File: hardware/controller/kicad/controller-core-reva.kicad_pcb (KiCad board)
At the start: 2 copper layers, 141.6 x 135.2 mm, 159 parts, among them J101 12V_ISOLATED_INPUT / JST XH, J102 STM_SWD / 1x6 2.54mm, J103 ESP_UART / 1x6 2.54mm, J104 UI_LINK / IDC 2x8 2.54mm, J105 JP13 NTC / 2 vías, J106 JP5 FLOW ADAPTER / VCC-GND-OC, J107 JP14 DOOR / contacto seco, J108 JP16 VISUAL V1..V8 / XH-8, J109 JP22 WATER / RED-WHITE-BLACK, J110 USB-C SERVICE / USB 2.0, J111 USB BENCH POWER / OPEN, J112 24V_ACTUATOR_INPUT / JST XH, J113 JP3 VALVE / JST XH, J114 POWER MONITOR / MEASURE ONLY, J115 JP8 GRINDER / 320VDC, J117 JP24 PUMP / 230VAC, J118 JP17 MAINS / L-N, J121 24V INTERNAL SELECT / OPEN FO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, K701 G5RL-1A-E-TV8 DC24, Q501 SI2308A, Q701 SI2308A / relay coil, U101 STM32G431RBT6, U201 ESP32-S3-WROOM-1U-N8R8, U203 USBLC6-2SC6, U301 AP63203WU-7, U302 TPS22918DBVR, U303 AP63200WU-7 / 24V to 12V, U501 DRV8876PWPR, U502 UCC27517DBVR, U601 TPS3828-33DBVR, U602 SN74LVC2G08DCTR, U603 SN74LVC2G08DCTR

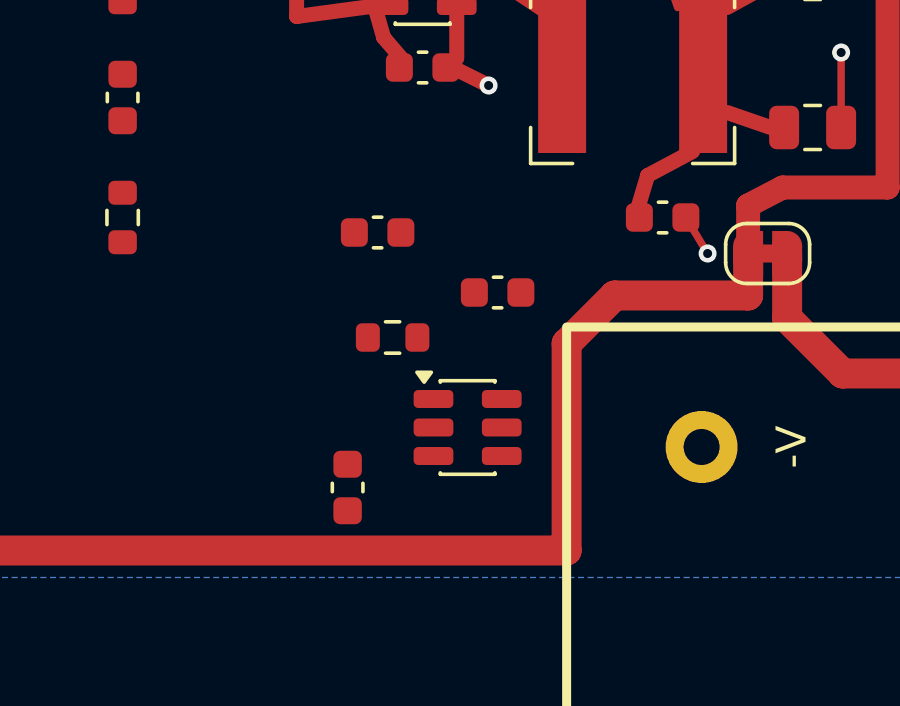
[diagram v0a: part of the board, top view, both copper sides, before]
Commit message: Route the front-panel load switch
PS701's footprint closes the pocket around U302 at x = 101.25 mm, so C307, C308
and C309 move west and north of the switch. C307 sets the rise time and sat
8 mm from pin 4; it is now beside it. The 3.3 V rail reaches the pocket along
y = 43 mm and down the free column at x = 91.6 mm.

DRC clean; 117 connections remain, down from 128.

Co-Authored-By: Claude Opus 5 <noreply@anthropic.com>
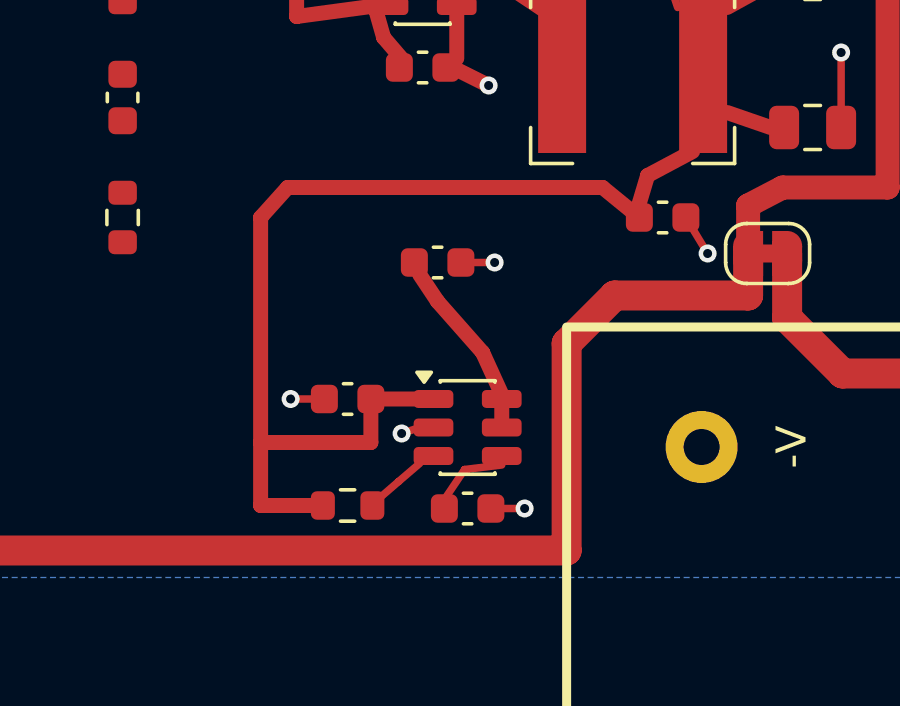
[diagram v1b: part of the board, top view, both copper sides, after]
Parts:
- moved C307 9.68 mm to (98.5, 53.7)
- moved R301 5.80 mm to (94.5, 53.6)
- moved C308 2.95 mm to (94.5, 50.0), turned to 180 degrees
- moved C309 2.24 mm to (97.5, 45.5)
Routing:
- net /3V3_CORE: track 112.4 -> 143.0 mm
- net /3V3_UI: track 0.00 -> 5.84 mm
- net /GND_UI: track 119.2 -> 123.2 mm, vias 70 -> 74
- net /UI_RISE: track 0.00 -> 2.45 mm
- net /UI_PWR_EN: track 0.00 -> 2.14 mm

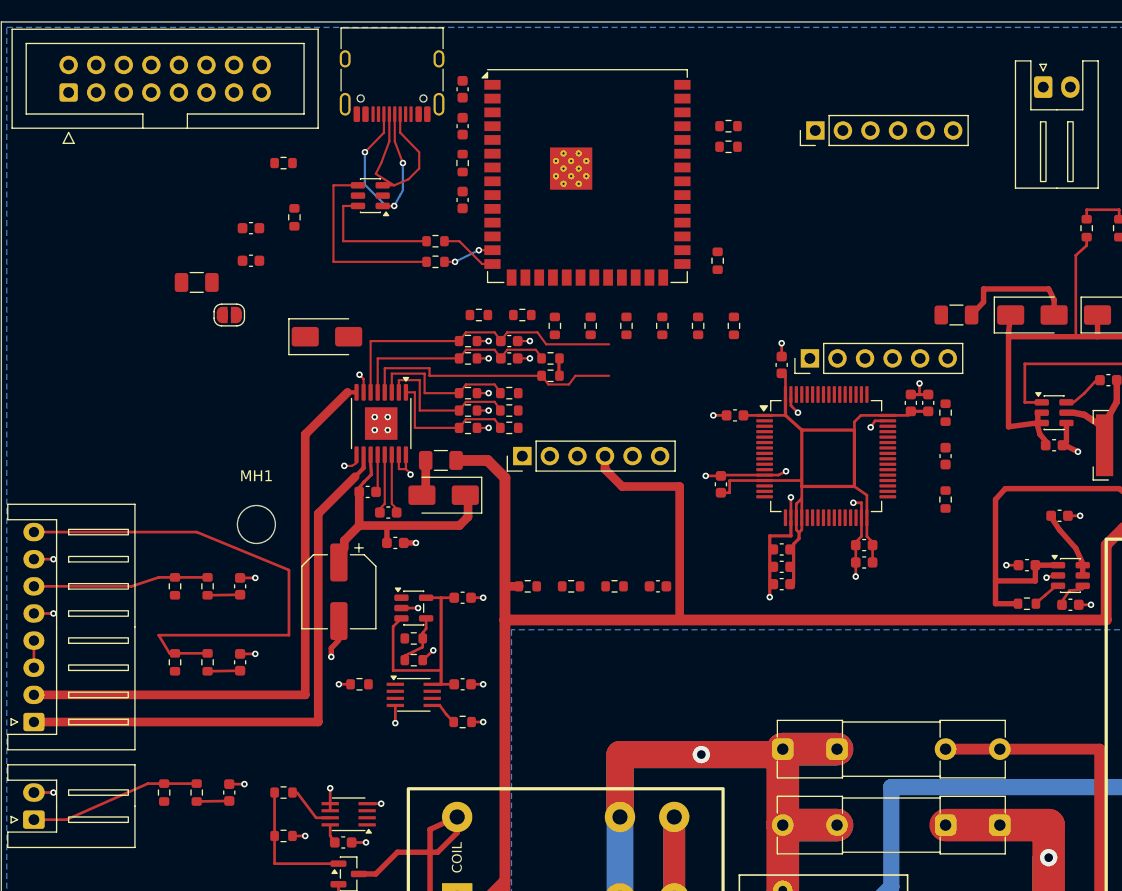
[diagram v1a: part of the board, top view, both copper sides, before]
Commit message: Distribute 3.3 V and ground the logic pins
One line leaves the buck along y = 43 mm and splits. The northern branch climbs
the gap between F301 and D301, runs over the ESP32 at y = 2.5 mm and feeds its
supply pins, its strap resistors and the UART header, plus the STM32 reset
pull-up and the SWD header. To free that gap, F301 moves 3 mm west and the
fused 12 V link passes under D301's body on B.Cu instead of round it.

The western branch runs in the 1.1 mm gap between the supervisor capacitors and
the 24 V trunk, passing under two 24 V branches on B.Cu, and reaches the
measurement header, the supervisor block, the arm gate and the contact and door
pull-ups. R405 turns 270 degrees so its supply pad faces north, clear of the
door harness lane.

Also drop the USB and ESP32 ground pins into the plane.

DRC clean; 90 connections remain, down from 117.

Co-Authored-By: Claude Opus 5 <noreply@anthropic.com>
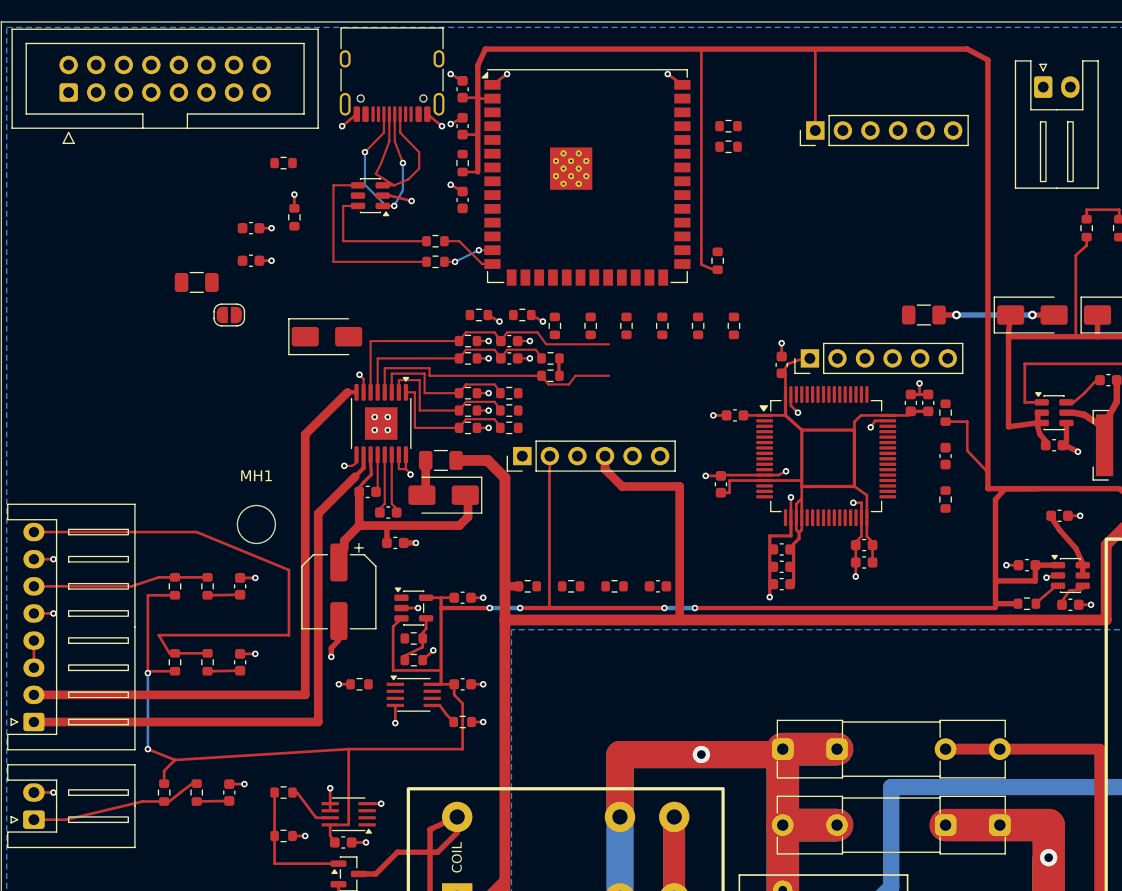
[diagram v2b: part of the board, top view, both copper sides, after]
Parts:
- moved F301 3.00 mm to (85.0, 27.0)
- turned R405 to -90 degrees
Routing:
- net /3V3_CORE: track 143.0 -> 414.9 mm, vias 0 -> 6
- net /GND_UI: track 123.2 -> 141.9 mm, vias 74 -> 87
- net /DOOR_RAW: track 15.7 -> 14.9 mm
- net /12V_FUSED: track 11.3 -> 10.6 mm, vias 0 -> 2

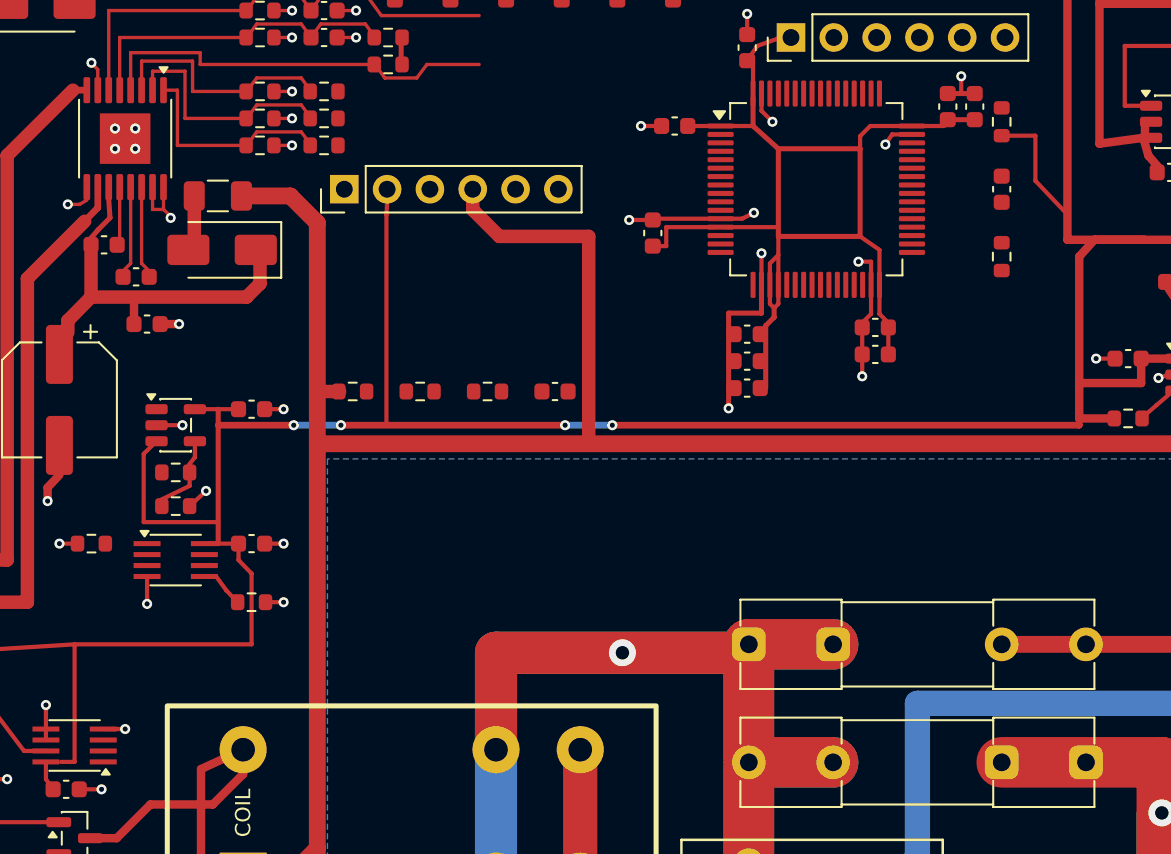
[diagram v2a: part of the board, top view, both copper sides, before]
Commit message: Route the reset tree
R101 and C101 sat east of the STM32, but its reset is pin 7 on the west side,
so the pair moves into the reset net's own corridor beside the supervisor that
drives it. The pin leaves flat, because the west pads are on a 0.5 mm pitch and
any diagonal touches its neighbour, drops to y = 50.5 mm and crosses west under
both 24 V branches into the 1.35 mm channel that was left empty for it.

Two reset points stay open and are documented: U602 pin 6, whose only approach
is the 0.87 mm gap east of the package that the valve arm net already uses, and
the SWD header's reset pin, which would have to cross the decoupling link north
of the MCU. Neither blocks debugging or start-up.

DRC clean; 85 connections remain.

Co-Authored-By: Claude Opus 5 <noreply@anthropic.com>
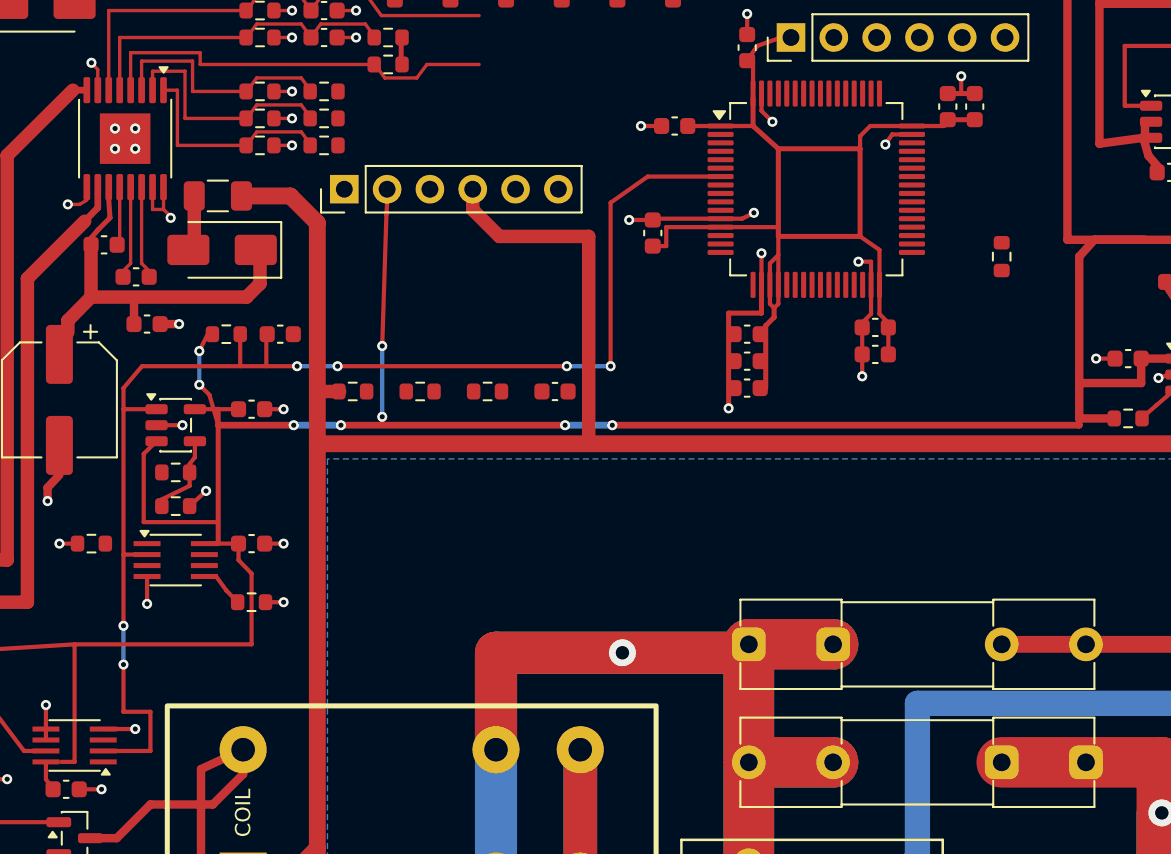
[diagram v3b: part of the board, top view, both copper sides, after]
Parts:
- moved R101 47.7 mm to (41.0, 48.6), turned to 0 degrees
- moved C101 43.7 mm to (44.2, 48.6), turned to 0 degrees
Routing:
- net /STM_NRST: track 0.00 -> 76.4 mm, vias 0 -> 6
- net /3V3_CORE: track 414.9 -> 413.7 mm, vias 6 -> 10
- net /GND_UI: track 141.9 -> 142.5 mm

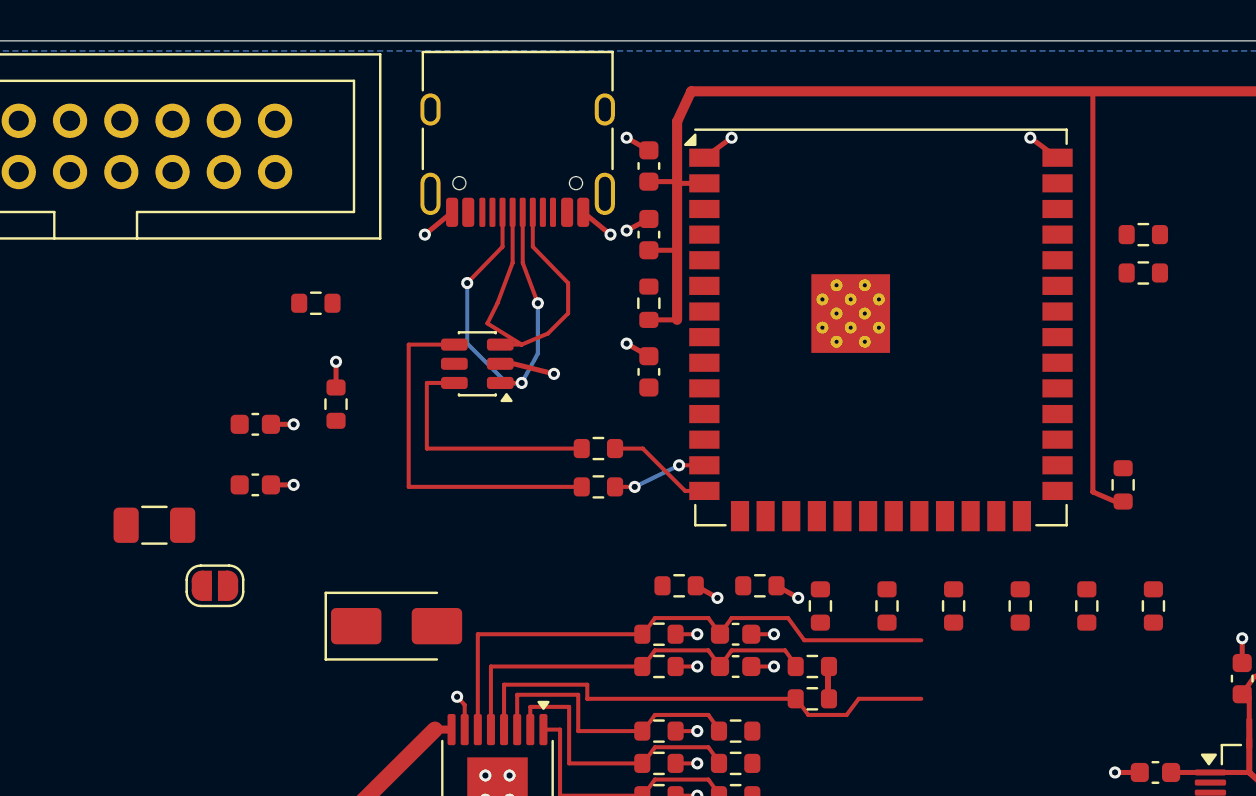
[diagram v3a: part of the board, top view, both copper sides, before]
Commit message: Route the service-USB rail
VBUS runs from the connector to the sense divider, the resettable fuse and the
bench-power jumper. The ESD part carries VBUS on the middle pin of its west
side with the protected pair leaving on either side, so that pin is reached on
B.Cu from the connector instead of through its own fanout. R202 turns 270
degrees so its supply pad faces north and the ESP32 boot strap leaves below it
without crossing.

DRC clean; 75 connections remain.

Co-Authored-By: Claude Opus 5 <noreply@anthropic.com>
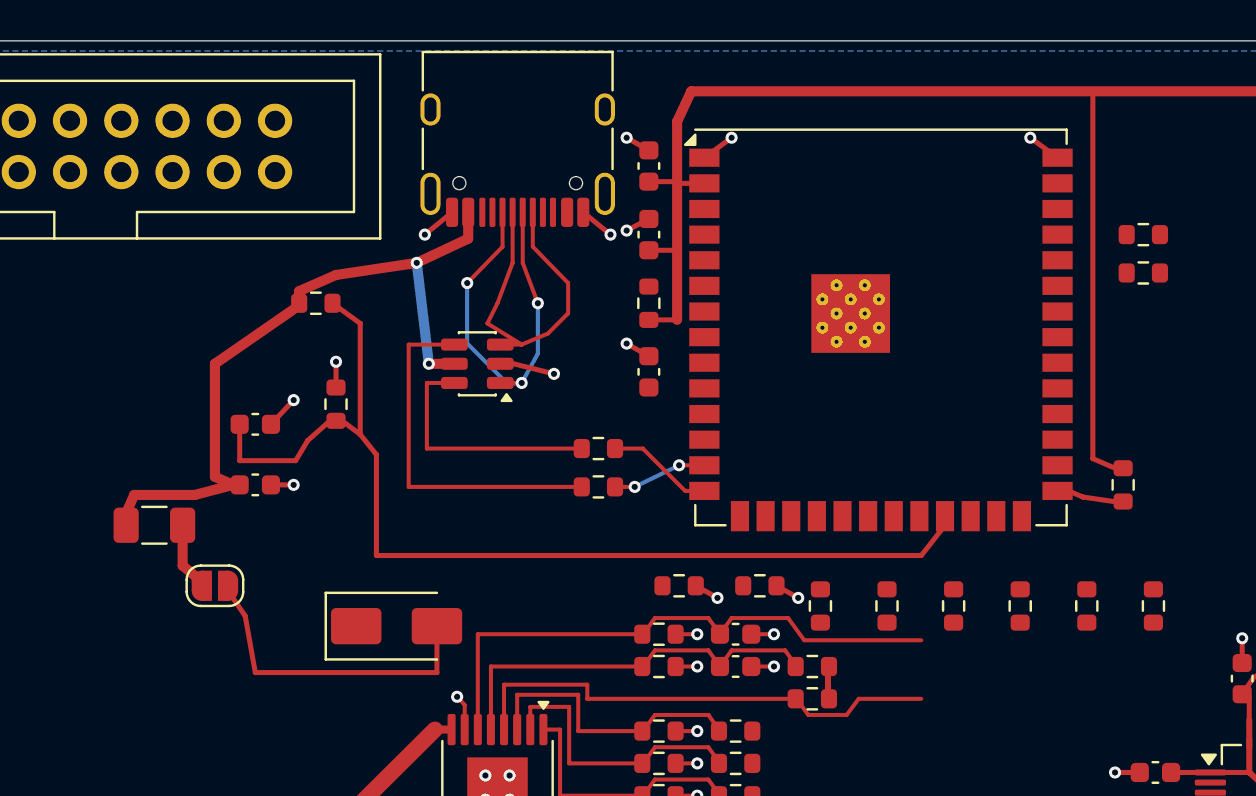
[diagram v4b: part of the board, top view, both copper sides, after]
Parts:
- turned R202 to -90 degrees
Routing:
- net /USB_VBUS_SENSE: track 0.00 -> 50.3 mm
- net /USB_VBUS: track 0.00 -> 33.5 mm, vias 0 -> 2
- net /USB_BENCH_ENABLE: track 0.00 -> 14.9 mm
- net /USB_VBUS_FUSED: track 0.00 -> 3.24 mm
- net /ESP_BOOT0: track 0.00 -> 2.30 mm
- net /3V3_CORE: track 413.7 -> 412.0 mm
- net /GND_UI: track 142.5 -> 143.0 mm
